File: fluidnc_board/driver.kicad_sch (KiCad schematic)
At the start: 37 parts

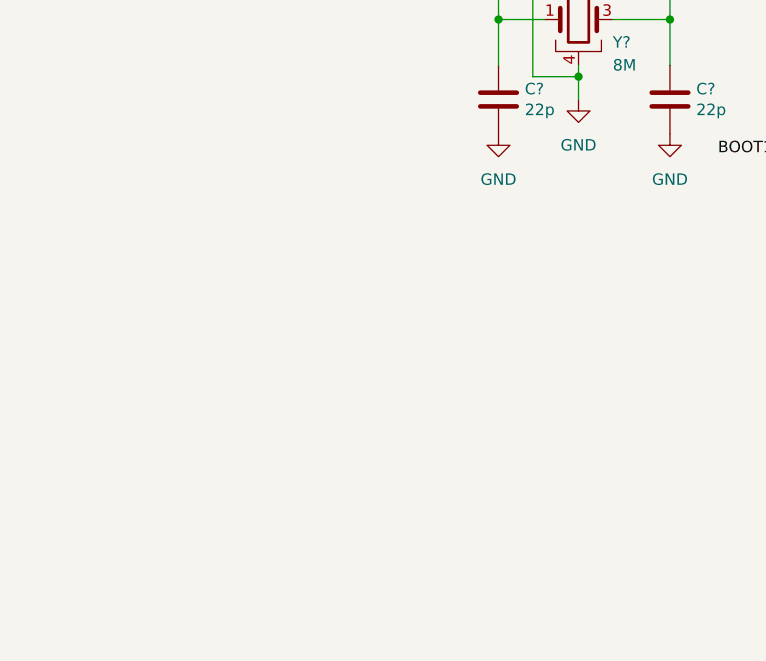
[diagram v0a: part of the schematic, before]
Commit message: outputs, spindle output and switch inputs
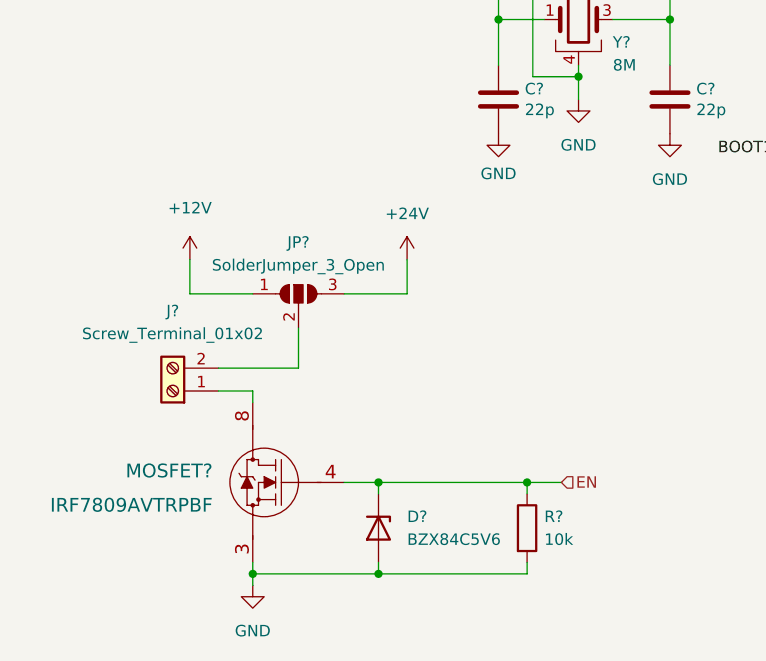
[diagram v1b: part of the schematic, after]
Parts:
- added D?: BZX84C5V6, Diode_SMD:D_SOT-23_ANK, symbol Diode:BZX84Cxx
- added J?: Screw_Terminal_01x02, symbol Connector:Screw_Terminal_01x02
- added JP?: SolderJumper_3_Open, symbol Jumper:SolderJumper_3_Open
- added MOSFET?: IRF7809AVTRPBF, SO-8_INF, symbol fluidnc_board:IRF7809AVTRPBF
- added R?: 10k, symbol Device:R
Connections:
- net EN: now also D?.1 (K), MOSFET?.4, R?.1
- net GND: now also D?.2 (A), MOSFET?.1, MOSFET?.2, MOSFET?.3, R?.2
- new net: J?.1 (Pin_1), MOSFET?.5, MOSFET?.6, MOSFET?.7, MOSFET?.8
- new net: J?.2 (Pin_2), JP?.2 (C)
- new net +12V: JP?.1 (A)
- new net +24V: JP?.3 (B)

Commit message: footprint associations and part no.
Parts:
- removed J?: BOOT1, Connector_PinHeader_2.54mm:PinHeader_1x03_P2.54mm_Vertical, symbol Connector:Conn_01x03_Male
- removed J?: BOOT0, Connector_PinHeader_2.54mm:PinHeader_1x03_P2.54mm_Vertical, symbol Connector:Conn_01x03_Male
- removed R? (x2): 2.2k, symbol Device:R
- removed R? (x2): 4.7k, symbol Device:R
- added C19: 100n, Capacitor_SMD:C_0603_1608Metric_Pad1.05x0.95mm_HandSolder, symbol Device:C
- added D13: LED, LED_SMD:LED_1206_3216Metric_Pad1.42x1.75mm_HandSolder, symbol Device:LED
- added JP5, JP6: SolderJumper_3_Bridged12, Jumper:SolderJumper-3_P1.3mm_Bridged12_RoundedPad1.0x1.5mm_NumberLabels, symbol Jumper:SolderJumper_3_Bridged12
- added R12, R13: 270, Resistor_SMD:R_0805_2012Metric_Pad1.15x1.40mm_HandSolder, symbol Device:R
- added R15, R16: 1k, Resistor_SMD:R_1206_3216Metric_Pad1.30x1.75mm_HandSolder, symbol Device:R
- added R17: 100, Resistor_SMD:R_0603_1608Metric_Pad0.98x0.95mm_HandSolder, symbol Device:R
- added U7: HCPL-0630, Package_SO:SOIC-8_3.9x4.9mm_P1.27mm, symbol Isolator:HCPL-0630
- C17, C18: renamed from C?; footprint (none) -> Capacitor_SMD:C_0603_1608Metric_Pad1.05x0.95mm_HandSolder; Digikey Part No. (none) -> 1276-1941-1-ND
- C20, C21: renamed from C?; footprint Capacitor_SMD:C_0805_2012Metric_Pad1.18x1.45mm_HandSolder -> Capacitor_SMD:C_0603_1608Metric_Pad1.08x0.95mm_HandSolder; Digi-Key Part Number 587-4388-1-ND -> (none); Digikey Part No. (none) -> 1276-2228-1-ND
- C22: renamed from C?; footprint Capacitor_SMD:C_0603_1608Metric_Pad1.08x0.95mm_HandSolder -> Capacitor_SMD:C_0402_1005Metric_Pad0.74x0.62mm_HandSolder; Digi-Key Part Number 587-4429-1-ND -> (none); Digikey Part No. (none) -> 1276-6640-1-ND
- C23, C24, C25, C26: renamed from C?; footprint Capacitor_SMD:C_0603_1608Metric_Pad1.08x0.95mm_HandSolder -> Capacitor_SMD:C_0603_1608Metric_Pad1.05x0.95mm_HandSolder; Digi-Key Part Number 587-1245-1-ND -> (none); Digikey Part No. (none) -> 1276-1941-1-ND
- C27: renamed from C?; Digi-Key Part Number 587-1779-1-ND -> (none); Digikey Part No. (none) -> 1276-1852-1-ND
- C28: renamed from C?; value 22u -> 4.7u; footprint (none) -> Capacitor_SMD:C_0805_2012Metric_Pad1.18x1.45mm_HandSolder; Digikey Part No. (none) -> 1276-1248-1-ND
- C29: renamed from C?; footprint (none) -> Capacitor_SMD:CP_Elec_10x10; Digikey Part No. (none) -> UCD1H101MCL6CT-ND
- D12: renamed from D?; Digikey Part No. (none) -> 1514-BZX84C5V6TRPBFREECT-ND
- J10: renamed from J?; footprint (none) -> Connector_Phoenix_MC:PhoenixContact_MC_1,5_4-G-3.81_1x04_P3.81mm_Horizontal
- J7: renamed from J?; footprint (none) -> Connector_Phoenix_MC:PhoenixContact_MC_1,5_2-G-3.81_1x02_P3.81mm_Horizontal
- J8: renamed from J?; footprint (none) -> Connector_JST:JST_XH_B6B-XH-A_1x06_P2.50mm_Vertical
- JP4: renamed from JP?; footprint (none) -> Jumper:SolderJumper-3_P1.3mm_Open_RoundedPad1.0x1.5mm_NumberLabels
- Q2: renamed from MOSFET?; footprint SO-8_INF -> Package_SO:SO-8_3.9x4.9mm_P1.27mm; Digikey Part No. (none) -> IRF7809AVPBFCT-ND
- R14: renamed from R?; footprint (none) -> Resistor_SMD:R_0805_2012Metric_Pad1.20x1.40mm_HandSolder; Digikey Part No. (none) -> 311-10KARCT-ND
- R18: renamed from R?; Digi-Key Part Number 311-10KARCT-ND -> (none); Digikey Part No. (none) -> 311-10KARCT-ND
- R19, R20: renamed from R?; footprint Resistor_SMD:R_0603_1608Metric_Pad1.05x0.95mm_HandSolder -> Resistor_SMD:R_0603_1608Metric_Pad0.98x0.95mm_HandSolder; Digi-Key Part Number 311-100KGRCT-ND -> (none); Digikey Part No. (none) -> 311-100KGRCT-ND
- SW2: renamed from SW?; Digi-Key Part Number EG2526CT-ND -> (none); Digikey Part No. (none) -> EG2526CT-ND
- U6: renamed from U?; Digikey Part No. (none) -> 505-ADG3304BRUZ-ND
- U8: renamed from U?; Digi-Key Part Number 497-6063-ND -> (none); Digikey Part No. (none) -> 497-6063-ND
- U9: renamed from U?; MANUFACTURER Trinamic -> (none); MAXIMUM_PACKAGE_HEIGHT N/A -> (none); PARTREV v11 -> (none); STANDARD Manufacturer Recommendations -> (none)
- Y2: renamed from Y?; Digi-Key Part Number 50-ECS-80-18-33-JGN-CT-ND -> (none); Digikey Part No. (none) -> 50-ECS-80-18-33-JGN-CT-ND
- gave numbers to parts that had none: 9
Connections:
- net +3V3: now also C19.2, JP5.1 (A), JP6.1 (A), R15.1, R16.1, R17.1, U7.8 (VCC)
- net +5V: no longer J8.6 (Pin_6)
- net BOOT0: now also JP5.2 (C)
- net BOOT1: now also JP6.2 (C)
- net ENC_A: now also R16.2, U7.7 (VO1)
- net ENC_B: now also R15.2, U7.6 (VO2)
- net GND: now also C19.1, JP5.3 (B), JP6.3 (B), U7.5 (GND); no longer J8.1 (Pin_1)
- net at J8.5 (Pin_5): now also R12.2
- net LED_IND: now reaches U8.2 (PC13)
- net LED_IND: now also D13.1 (K)
- net at J8.2 (Pin_2): now also U7.4 (A2)
- net at J8.3 (Pin_3): now also R13.2
- net at J8.4 (Pin_4): now also U7.2 (C1)
- new net: R12.1, U7.1 (A1)
- new net: D13.2 (A), R17.2
- new net: R13.1, U7.3 (C2)
- new net 5V_ISO: J8.6 (Pin_6)
- new net GND_ISO: J8.1 (Pin_1)
- no-connect marks 30 -> 29
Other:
- moved on the sheet: C17, C18, C20, C21, C22, D12, J7, J8, JP4, Q2, R14, R18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

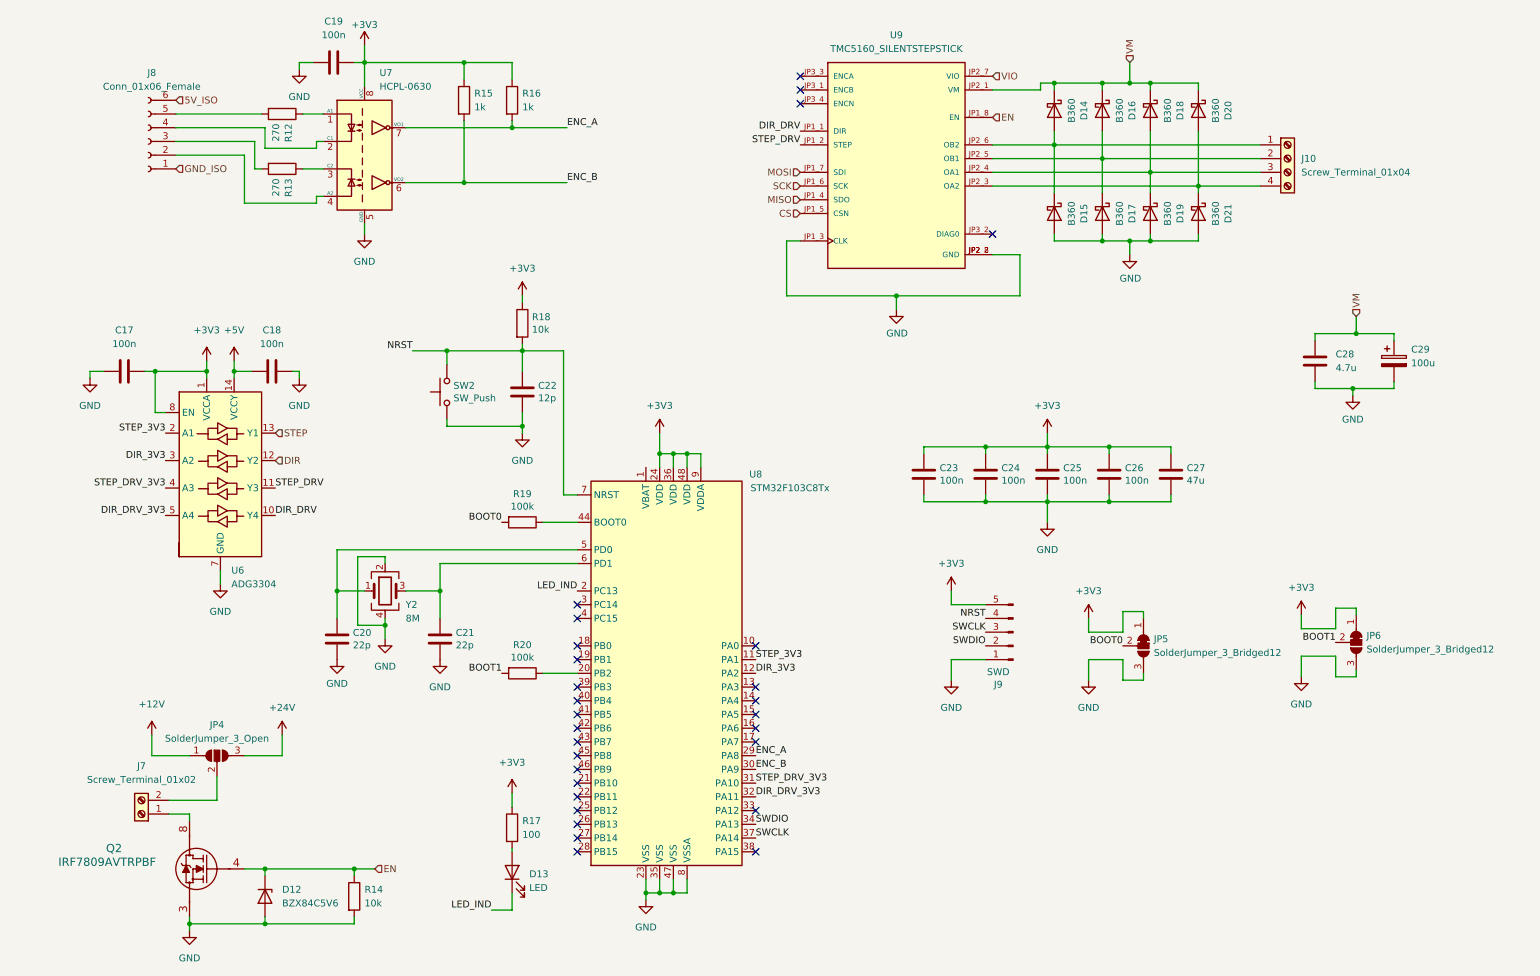
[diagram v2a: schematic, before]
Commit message: fix some footprint associations
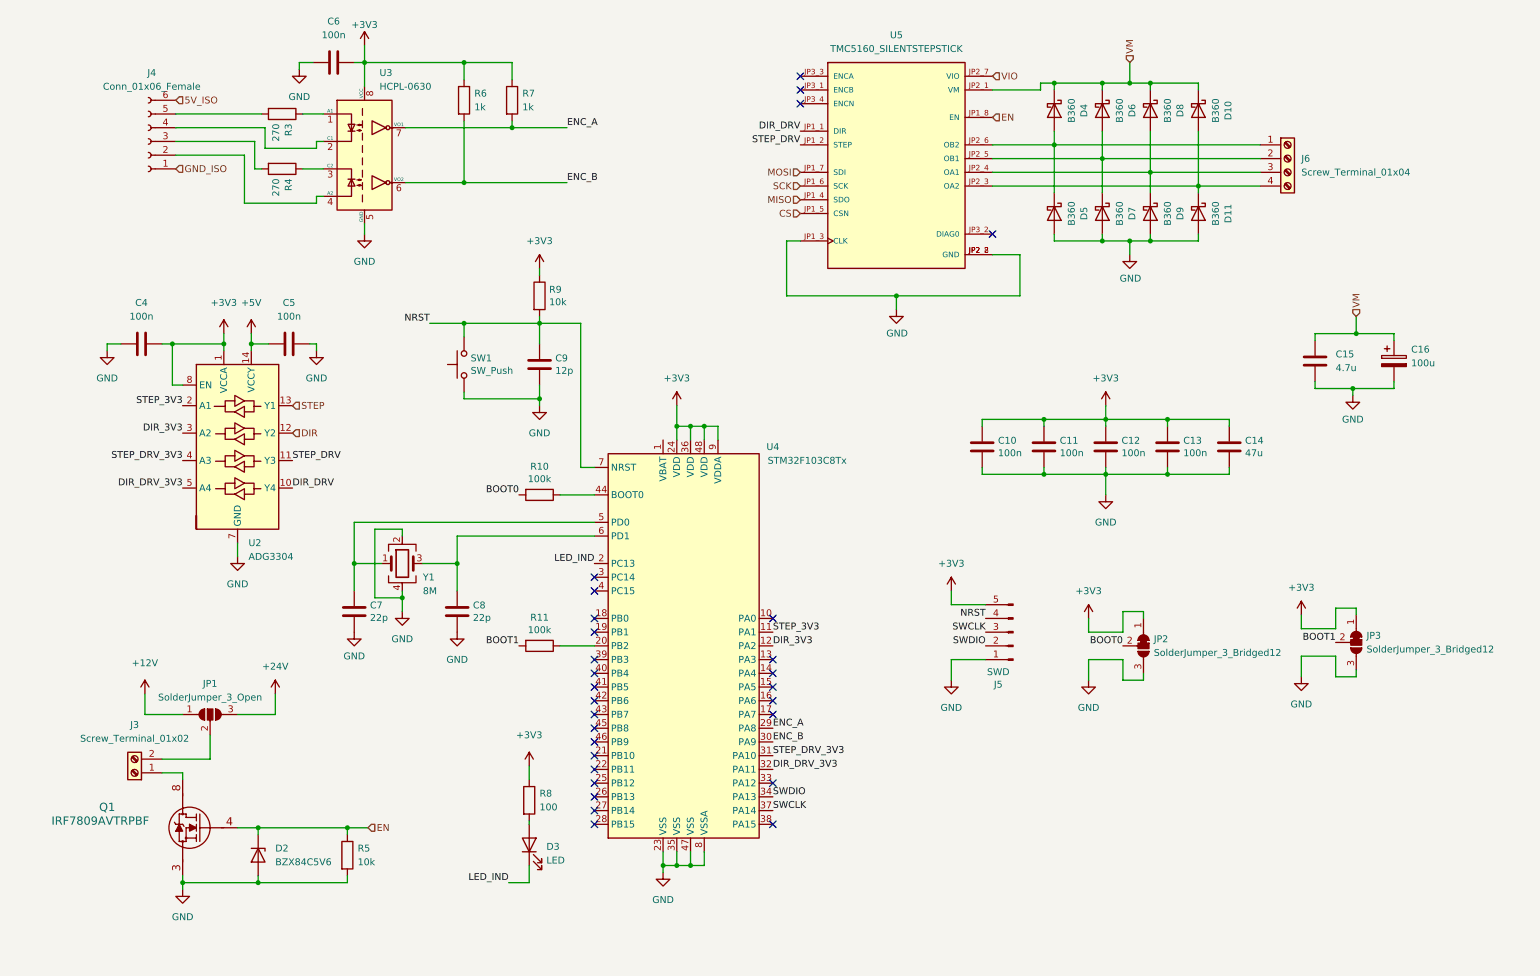
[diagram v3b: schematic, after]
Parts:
- U5: renamed from U9; footprint grbl_board:TMC5160_SILENTSTEPSTICK -> fluidnc_board:TMC5160_SILENTSTEPSTICK
- renumbered C23 to C10, C24 to C11, C25 to C12, C26 to C13, C27 to C14, C28 to C15, C29 to C16, C17 to C4, C18 to C5, C19 to C6, C20 to C7, C21 to C8, C22 to C9, D20 to D10, D21 to D11, D12 to D2, D13 to D3, D14 to D4, D15 to D5, D16 to D6, D17 to D7, D18 to D8, D19 to D9, J7 to J3, J8 to J4, J9 to J5, J10 to J6, JP4 to JP1, JP5 to JP2, JP6 to JP3, Q2 to Q1, R19 to R10, R20 to R11, R12 to R3, R13 to R4, R14 to R5, R15 to R6, R16 to R7, R17 to R8, R18 to R9, SW2 to SW1, U6 to U2, U7 to U3, U8 to U4, Y2 to Y1
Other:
- moved on the sheet: C10, C11, C12, C13, C14, C4, C5, C7, C8, C9, D2, D3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
